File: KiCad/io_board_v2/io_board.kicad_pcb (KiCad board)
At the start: 4 copper layers, 119.1 x 99.1 mm, 87 parts, among them J1 RS232, J2 Keyboard, J3 SD_Card, J4 JTAG, J5 DS1307, J6 BME280, J7 I²C, U1 ST16C550CJ44, U12 AMS1117-3.3, U13 SN74LVC245A, U15 SN74LVC8T245PWR, U17 PCA9564D, U18 24C04, U19 SN74AVC8T245PW, U2 MAX232, U3 74HC07, U4 74HCT04, U5 8042, U6 MicroSD_SPI_CD, U7 EPM240T100, U8 74HCT04, U9 SN74LVC245A, X1 Edge72, X2 20 MHz, Y1 8 MHz

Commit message: Fixed wrong Mini-DIN 6 footprint.
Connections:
- J2 pad 1: /PS2/KBD_CLK -> /PS2/KBD_DATA
- J2 pad 2: GND -> Net-(J2-Pad2)
- J2 pad 3: /PS2/KBD_DATA -> GND
- J2 pad 4: Net-(J2-Pad4) -> VCC
- J2 pad 5: VCC -> /PS2/KBD_CLK
- U6 pad : GND -> (no net)
- U6 pad 10: GND -> (no net)
- U6 pad ~: GND -> (no net)
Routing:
- net GND: vias 131 -> 127
- net (no net): vias 0 -> 4

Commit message: Fixed I/O board issues.
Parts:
- moved C8 1.67 mm to (135.5, 58.0)
- moved C9 1.67 mm to (135.5, 63.4)
- moved C7 1.67 mm to (135.5, 68.7)
- moved R4 1.67 mm to (132.5, 58.0)
- moved C12 1.67 mm to (132.5, 63.4)
- moved R5 1.67 mm to (132.5, 68.7)
- moved J2 1.53 mm to (143.8, 62.7)
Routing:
- net /PS2/KBD_DATA: track 123.4 -> 126.1 mm, vias 2 -> 1
- net VCC: track 426.7 -> 425.3 mm
- net /PS2/KBD_CLK: track 139.2 -> 138.7 mm

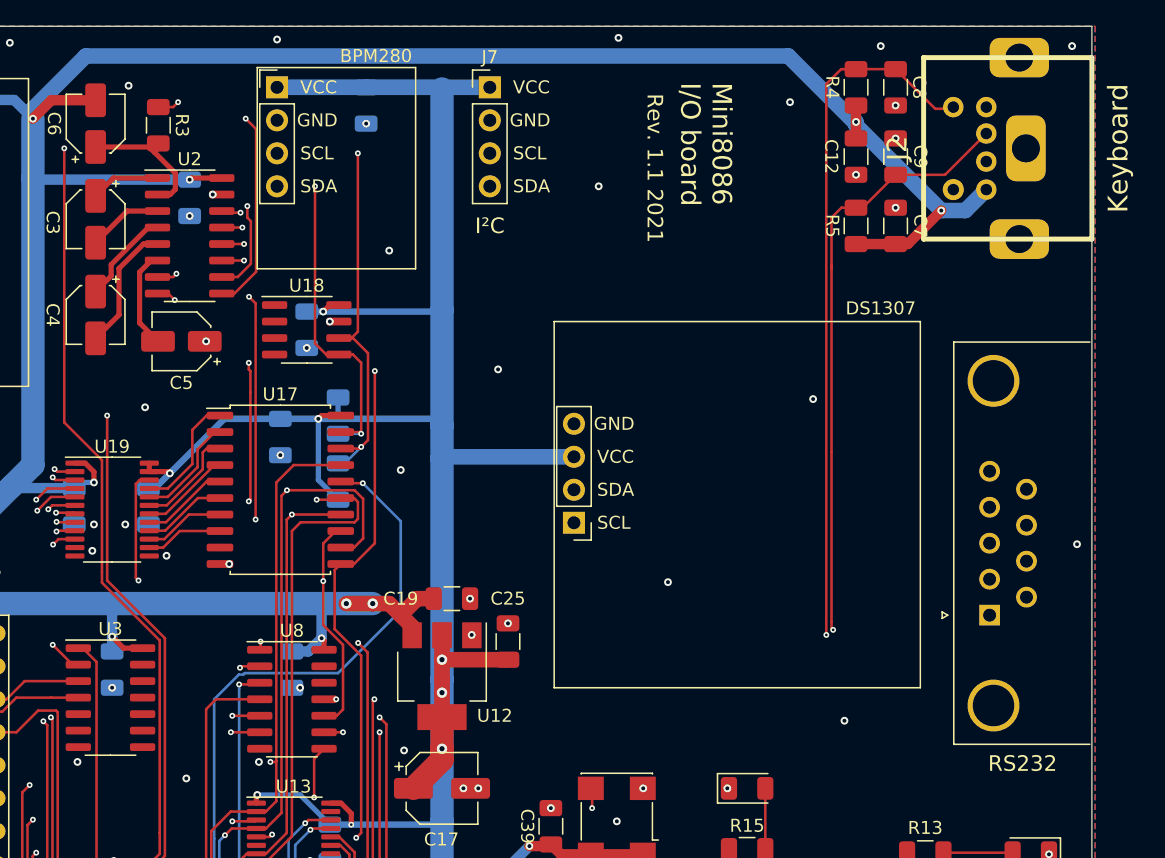
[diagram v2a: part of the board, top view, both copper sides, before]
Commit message: Minor changes at I/O board, LED board and VGA
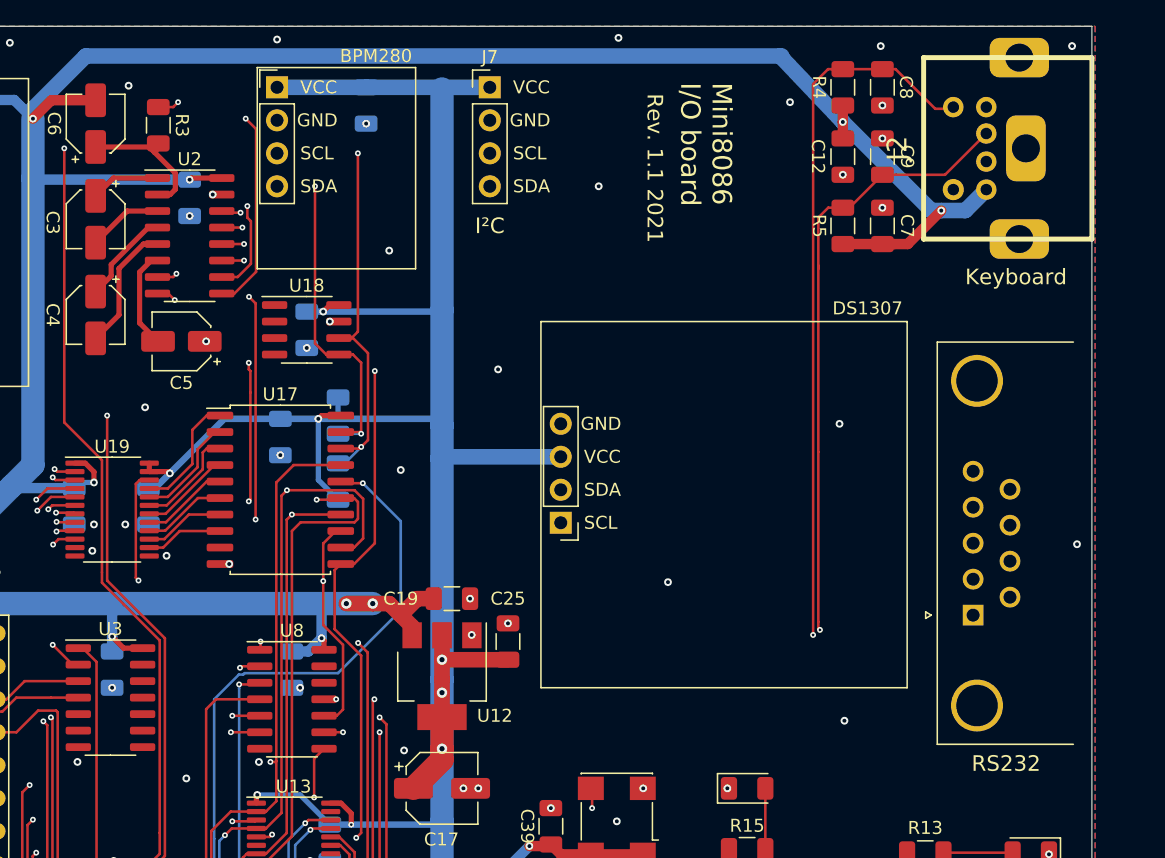
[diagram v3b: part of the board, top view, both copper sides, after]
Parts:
- moved J1 1.27 mm to (141.5, 98.7)
- moved C12 1.02 mm to (131.4, 63.4)
- moved R4 1.02 mm to (131.4, 58.0)
- moved R5 1.02 mm to (131.4, 68.7)
- moved J5 1.02 mm to (109.7, 91.6)
- moved C7 1.02 mm to (134.5, 68.7)
- moved C8 1.02 mm to (134.5, 58.0)
- moved C9 1.02 mm to (134.5, 63.4)
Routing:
- net VCC: track 425.3 -> 427.3 mm
- net Net-(J1-Pad4): track 81.1 -> 79.8 mm
- net VCC3: track 378.0 -> 377.0 mm
- net SDA: track 113.2 -> 112.1 mm
- net SCL: track 118.2 -> 117.2 mm
- net /serial/RX: track 74.0 -> 73.5 mm
- net /serial/CTS: track 86.1 -> 85.6 mm
- net /serial/RTS: track 82.0 -> 81.5 mm

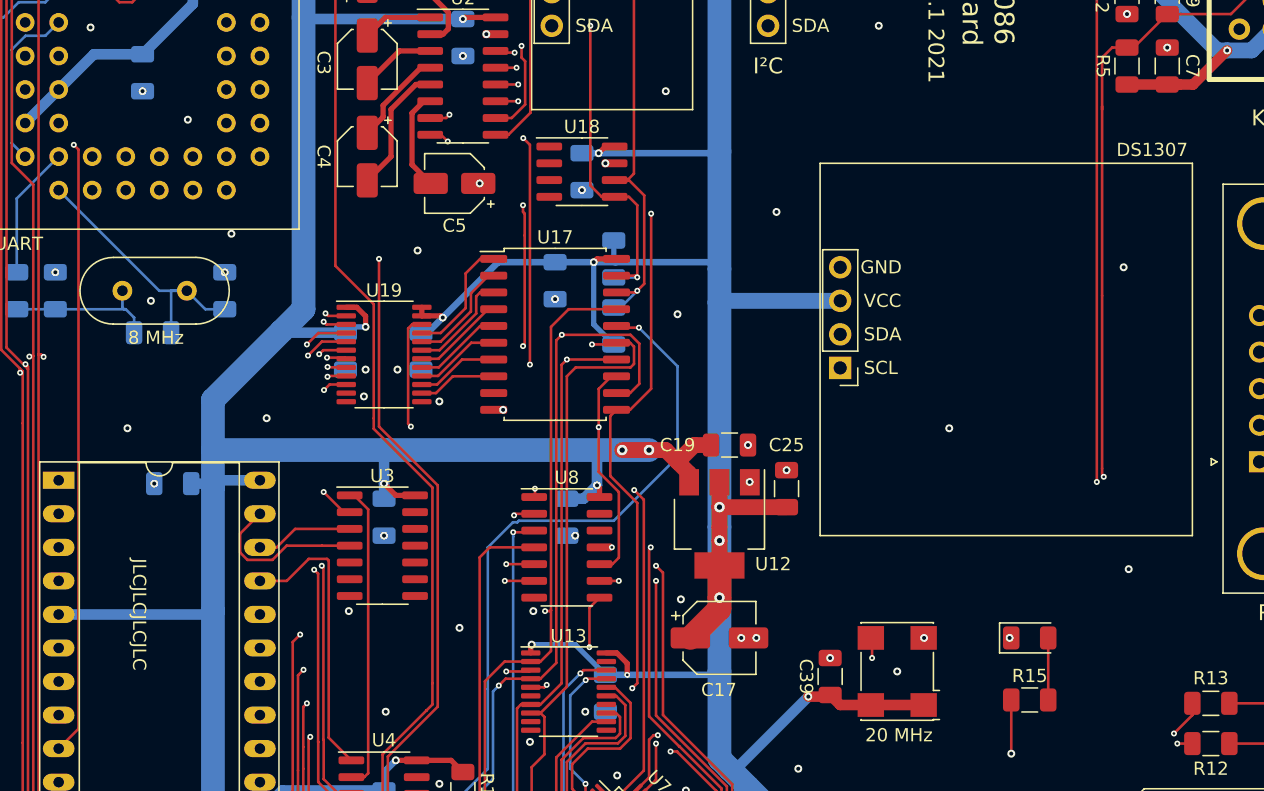
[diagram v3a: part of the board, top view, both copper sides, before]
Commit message: Migration from KiCad 5 to KiCad 7
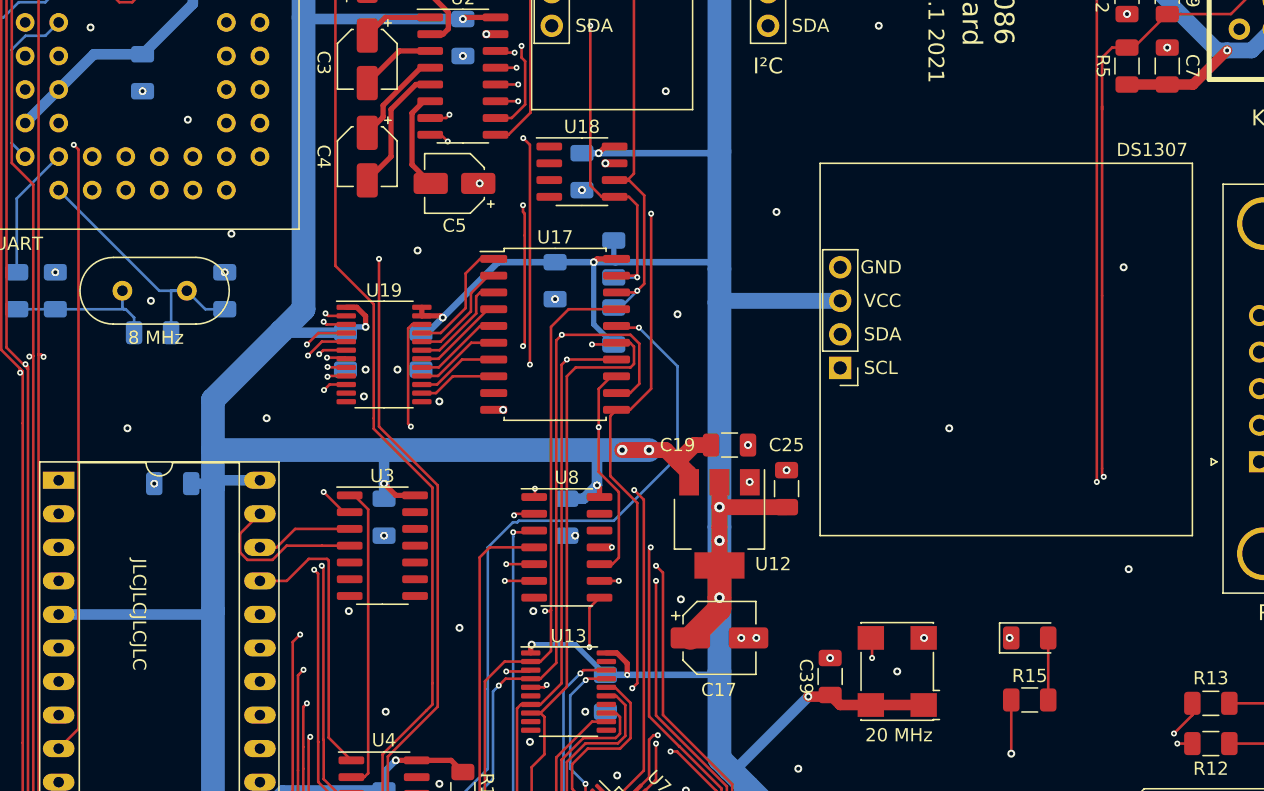
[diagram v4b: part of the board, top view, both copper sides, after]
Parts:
- R12, R13, R15: value 100 -> 120
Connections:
- net /PS2/~PCLK renamed /PS2/~{PCLK}
- net /SD drive/M_~IO~_3 renamed /SD drive/M_~{IO}_3
- net /SD drive/~RD_3 renamed /SD drive/~{RD_3}
- net /SD drive/~RESET_3 renamed /SD drive/~{RESET_3}
- net /SD drive/~WR_3 renamed /SD drive/~{WR_3}
- net M_~IO renamed M_~{IO}
- net ~CS_8042 renamed ~{CS_8042}
- net ~CS_I2C renamed ~{CS_I2C}
- net ~CS_UART renamed ~{CS_UART}
- net ~D_EN renamed ~{D_EN}
- net ~INT_I2C renamed ~{INT_I2C}
- net ~RD renamed ~{RD}
- net ~RESET renamed ~{RESET}
- net ~SD_IRQ renamed ~{SD_IRQ}
- net ~WR renamed ~{WR}
- J1 pad 1: Net-(J1-Pad1) -> unconnected-(J1-Pad1)
- J1 pad 6: Net-(J1-Pad6) -> unconnected-(J1-Pad6)
- J1 pad 9: Net-(J1-Pad9) -> unconnected-(J1-Pad9)
- J2 pad 2: Net-(J2-Pad2) -> unconnected-(J2-Pad2)
- J2 pad 6: Net-(J2-Pad6) -> unconnected-(J2-Pad6)
- J3 pad 11: Net-(J3-Pad11) -> unconnected-(J3-WRITE_PROTECT-Pad11)
- J4 pad 6: Net-(J4-Pad6) -> unconnected-(J4-Pin_6-Pad6)
- J4 pad 7: Net-(J4-Pad7) -> unconnected-(J4-Pin_7-Pad7)
- J4 pad 8: Net-(J4-Pad8) -> unconnected-(J4-Pin_8-Pad8)
- U1 pad 1: Net-(U1-Pad1) -> unconnected-(U1-NC-Pad1)
- U1 pad 12: Net-(U1-Pad12) -> unconnected-(U1-NC-Pad12)
- U1 pad 23: Net-(U1-Pad23) -> unconnected-(U1-NC-Pad23)
- U1 pad 26: Net-(U1-Pad26) -> unconnected-(U1-~{DDIS}-Pad26)
- U1 pad 27: Net-(U1-Pad27) -> unconnected-(U1-~{TXRDY}-Pad27)
- U1 pad 32: Net-(U1-Pad32) -> unconnected-(U1-~{RXRDY}-Pad32)
- U1 pad 34: Net-(U1-Pad34) -> unconnected-(U1-NC-Pad34)
- U1 pad 35: Net-(U1-Pad35) -> unconnected-(U1-~{OP2}-Pad35)
- U1 pad 37: Net-(U1-Pad37) -> unconnected-(U1-~{DTR}-Pad37)
- U1 pad 38: Net-(U1-Pad38) -> unconnected-(U1-~{OP1}-Pad38)
- U13 pad 11: Net-(U13-Pad11) -> unconnected-(U13-B7-Pad11)
- U13 pad 14: Net-(U13-Pad14) -> unconnected-(U13-B4-Pad14)
- U13 pad 6: Net-(U13-Pad6) -> unconnected-(U13-A4-Pad6)
- U13 pad 9: Net-(U13-Pad9) -> unconnected-(U13-A7-Pad9)
- U17 pad 9: Net-(U17-Pad9) -> unconnected-(U17-NC-Pad9)
- U3 pad 10: Net-(U3-Pad10) -> unconnected-(U3-Pad10)
- U3 pad 12: Net-(U3-Pad12) -> unconnected-(U3-Pad12)
- U3 pad 6: Net-(U3-Pad6) -> unconnected-(U3-Pad6)
- U3 pad 8: Net-(U3-Pad8) -> unconnected-(U3-Pad8)
- U4 pad 12: Net-(U4-Pad12) -> unconnected-(U4-Pad12)
- U4 pad 6: Net-(U4-Pad6) -> unconnected-(U4-Pad6)
- U5 pad 11: Net-(U5-Pad11) -> unconnected-(U5-ALE-Pad11)
- U5 pad 21: Net-(U5-Pad21) -> unconnected-(U5-P2.0-Pad21)
- U5 pad 22: Net-(U5-Pad22) -> unconnected-(U5-P2.1-Pad22)
- U5 pad 23: Net-(U5-Pad23) -> unconnected-(U5-P2.2-Pad23)
- U5 pad 24: Net-(U5-Pad24) -> unconnected-(U5-P2.3-Pad24)
- U5 pad 27: Net-(U5-Pad27) -> unconnected-(U5-P1.0-Pad27)
- U5 pad 28: Net-(U5-Pad28) -> unconnected-(U5-P1.1-Pad28)
- U5 pad 29: Net-(U5-Pad29) -> unconnected-(U5-P1.2-Pad29)
- U5 pad 30: Net-(U5-Pad30) -> unconnected-(U5-P1.3-Pad30)
- U5 pad 31: Net-(U5-Pad31) -> unconnected-(U5-P1.4-Pad31)
- U5 pad 32: Net-(U5-Pad32) -> unconnected-(U5-P1.5-Pad32)
- U5 pad 33: Net-(U5-Pad33) -> unconnected-(U5-P1.6-Pad33)
- U5 pad 34: Net-(U5-Pad34) -> unconnected-(U5-P1.7-Pad34)
- U5 pad 36: Net-(U5-Pad36) -> unconnected-(U5-P2.5-Pad36)
- U7 pad 1: Net-(U7-Pad1) -> unconnected-(U7-IO2_1-Pad1)
- U7 pad 14: Net-(U7-Pad14) -> unconnected-(U7-IO1_14/GCLK1-Pad14)
- U7 pad 15: Net-(U7-Pad15) -> unconnected-(U7-IO1_15-Pad15)
- U7 pad 16: Net-(U7-Pad16) -> unconnected-(U7-IO1_16-Pad16)
- U7 pad 17: Net-(U7-Pad17) -> unconnected-(U7-IO1_17-Pad17)
- U7 pad 18: Net-(U7-Pad18) -> unconnected-(U7-IO1_18-Pad18)
- U7 pad 19: Net-(U7-Pad19) -> unconnected-(U7-IO1_19-Pad19)
- U7 pad 2: Net-(U7-Pad2) -> unconnected-(U7-IO1_2-Pad2)
- U7 pad 20: Net-(U7-Pad20) -> unconnected-(U7-IO1_20-Pad20)
- U7 pad 21: Net-(U7-Pad21) -> unconnected-(U7-IO1_21-Pad21)
- U7 pad 26: Net-(U7-Pad26) -> unconnected-(U7-IO1_26-Pad26)
- U7 pad 37: Net-(U7-Pad37) -> unconnected-(U7-IO1_37-Pad37)
- U7 pad 38: Net-(U7-Pad38) -> unconnected-(U7-IO1_38-Pad38)
- U7 pad 39: Net-(U7-Pad39) -> unconnected-(U7-IO1_39-Pad39)
- U7 pad 52: Net-(U7-Pad52) -> unconnected-(U7-IO2_52-Pad52)
- U7 pad 54: Net-(U7-Pad54) -> unconnected-(U7-IO2_54-Pad54)
- U7 pad 55: Net-(U7-Pad55) -> unconnected-(U7-IO2_55-Pad55)
- U7 pad 56: Net-(U7-Pad56) -> unconnected-(U7-IO2_56-Pad56)
- U7 pad 57: Net-(U7-Pad57) -> unconnected-(U7-IO2_57-Pad57)
- U7 pad 58: Net-(U7-Pad58) -> unconnected-(U7-IO2_58-Pad58)
- U7 pad 6: Net-(U7-Pad6) -> unconnected-(U7-IO1_6-Pad6)
- U7 pad 61: Net-(U7-Pad61) -> unconnected-(U7-IO2_61-Pad61)
- U7 pad 62: Net-(U7-Pad62) -> unconnected-(U7-IO2_62/GCLK2-Pad62)
- U7 pad 64: Net-(U7-Pad64) -> unconnected-(U7-IO2_64/GCLK3-Pad64)
- U7 pad 66: Net-(U7-Pad66) -> unconnected-(U7-IO2_66-Pad66)
- U7 pad 67: Net-(U7-Pad67) -> unconnected-(U7-IO2_67-Pad67)
- U7 pad 68: Net-(U7-Pad68) -> unconnected-(U7-IO2_68-Pad68)
- U7 pad 69: Net-(U7-Pad69) -> unconnected-(U7-IO2_69-Pad69)
- U7 pad 74: Net-(U7-Pad74) -> unconnected-(U7-IO2_74-Pad74)
- U7 pad 75: Net-(U7-Pad75) -> unconnected-(U7-IO2_75-Pad75)
- U7 pad 76: Net-(U7-Pad76) -> unconnected-(U7-IO2_76-Pad76)
- U7 pad 77: Net-(U7-Pad77) -> unconnected-(U7-IO2_77-Pad77)
- U7 pad 78: Net-(U7-Pad78) -> unconnected-(U7-IO2_78-Pad78)
- U7 pad 84: Net-(U7-Pad84) -> unconnected-(U7-IO2_84-Pad84)
- U7 pad 85: Net-(U7-Pad85) -> unconnected-(U7-IO2_85-Pad85)
- U7 pad 86: Net-(U7-Pad86) -> unconnected-(U7-IO2_86-Pad86)
- U7 pad 88: Net-(U7-Pad88) -> unconnected-(U7-IO2_88-Pad88)
- U7 pad 89: Net-(U7-Pad89) -> unconnected-(U7-IO2_89-Pad89)
- U7 pad 90: Net-(U7-Pad90) -> unconnected-(U7-IO2_90-Pad90)
- U7 pad 91: Net-(U7-Pad91) -> unconnected-(U7-IO2_91-Pad91)
- U7 pad 92: Net-(U7-Pad92) -> unconnected-(U7-IO2_92-Pad92)
- U7 pad 95: Net-(U7-Pad95) -> unconnected-(U7-IO2_95-Pad95)
- U7 pad 96: Net-(U7-Pad96) -> unconnected-(U7-IO2_96-Pad96)
- U7 pad 97: Net-(U7-Pad97) -> unconnected-(U7-IO2_97-Pad97)
- U8 pad 12: Net-(U8-Pad12) -> unconnected-(U8-Pad12)
- X1 pad 16: Net-(X1-Pad16) -> unconnected-(X1-A11-Pad16)
- X1 pad 17: Net-(X1-Pad17) -> unconnected-(X1-A12-Pad17)
- X1 pad 18: Net-(X1-Pad18) -> unconnected-(X1-A13-Pad18)
- X1 pad 19: Net-(X1-Pad19) -> unconnected-(X1-A14-Pad19)
- X1 pad 20: Net-(X1-Pad20) -> unconnected-(X1-A15-Pad20)
- X1 pad 21: Net-(X1-Pad21) -> unconnected-(X1-A16-Pad21)
- X1 pad 22: Net-(X1-Pad22) -> unconnected-(X1-A17-Pad22)
- X1 pad 23: Net-(X1-Pad23) -> unconnected-(X1-A18-Pad23)
- X1 pad 24: Net-(X1-Pad24) -> unconnected-(X1-A19-Pad24)
- X1 pad 25: Net-(X1-Pad25) -> unconnected-(X1-N/C-Pad25)
- X1 pad 26: Net-(X1-Pad26) -> unconnected-(X1-~{VGA_IO}-Pad26)
- X1 pad 27: Net-(X1-Pad27) -> unconnected-(X1-~{VGA_MEM}-Pad27)
- X1 pad 28: Net-(X1-Pad28) -> unconnected-(X1-RDY1-Pad28)
- X1 pad 29: Net-(X1-Pad29) -> unconnected-(X1-RDY2-Pad29)
- X1 pad 31: Net-(X1-Pad31) -> unconnected-(X1-~{IO_DBG}-Pad31)
- X1 pad 32: Net-(X1-Pad32) -> unconnected-(X1-NMI-Pad32)
- X1 pad 33: Net-(X1-Pad33) -> unconnected-(X1-TMR2-Pad33)
- X1 pad 49: Net-(X1-Pad49) -> unconnected-(X1-D8-Pad49)
- X1 pad 50: Net-(X1-Pad50) -> unconnected-(X1-D9-Pad50)
- X1 pad 51: Net-(X1-Pad51) -> unconnected-(X1-D10-Pad51)
- X1 pad 52: Net-(X1-Pad52) -> unconnected-(X1-D11-Pad52)
- X1 pad 53: Net-(X1-Pad53) -> unconnected-(X1-D12-Pad53)
- X1 pad 54: Net-(X1-Pad54) -> unconnected-(X1-D13-Pad54)
- X1 pad 55: Net-(X1-Pad55) -> unconnected-(X1-D14-Pad55)
- X1 pad 56: Net-(X1-Pad56) -> unconnected-(X1-D15-Pad56)
- X1 pad 58: Net-(X1-Pad58) -> unconnected-(X1-IRQ3-Pad58)
- X1 pad 60: Net-(X1-Pad60) -> unconnected-(X1-IRQ5-Pad60)
- X1 pad 66: Net-(X1-Pad66) -> unconnected-(X1-~{BHE}-Pad66)
- X1 pad 67: Net-(X1-Pad67) -> unconnected-(X1-~{MEMRD}-Pad67)
- X1 pad 68: Net-(X1-Pad68) -> unconnected-(X1-~{MEMWR}-Pad68)
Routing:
- net VCC: track 427.3 -> 426.4 mm
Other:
- net class Default removed
